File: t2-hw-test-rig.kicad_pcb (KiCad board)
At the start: 2 copper layers, 86.4 x 94 mm, 150 parts, among them J101 CONN_01X02, J102 BARREL_JACK, J103 CONN_01X02, J201 MICROUSB-TH, J202 CONN_01X02, J203 MICROUSB-TH, J204 USB_A_TH, J301 CONN_02x05, 0.05", Q101 pMOS, Q401 CJ2302, Q402 CJ2302, Q403 CJ2302, Q404 CJ2302, SW301 Switch_DPST, SW302 Switch_DPST, U101 MAX6102, U102 XC6206P332MR-G, U301 ATSAMD21J18A-MUT, U302 AAT4610, U303 AAT4610, U401 MAX9919FASA+, U402 MAX9919FASA+, U403 MAX9919FASA+, U404 MAX9919FASA+, U405 MAX9919FASA+, U501 TSV324IDT, U502 TSV324IDT, U503 TSV324IDT, X301 FC-135

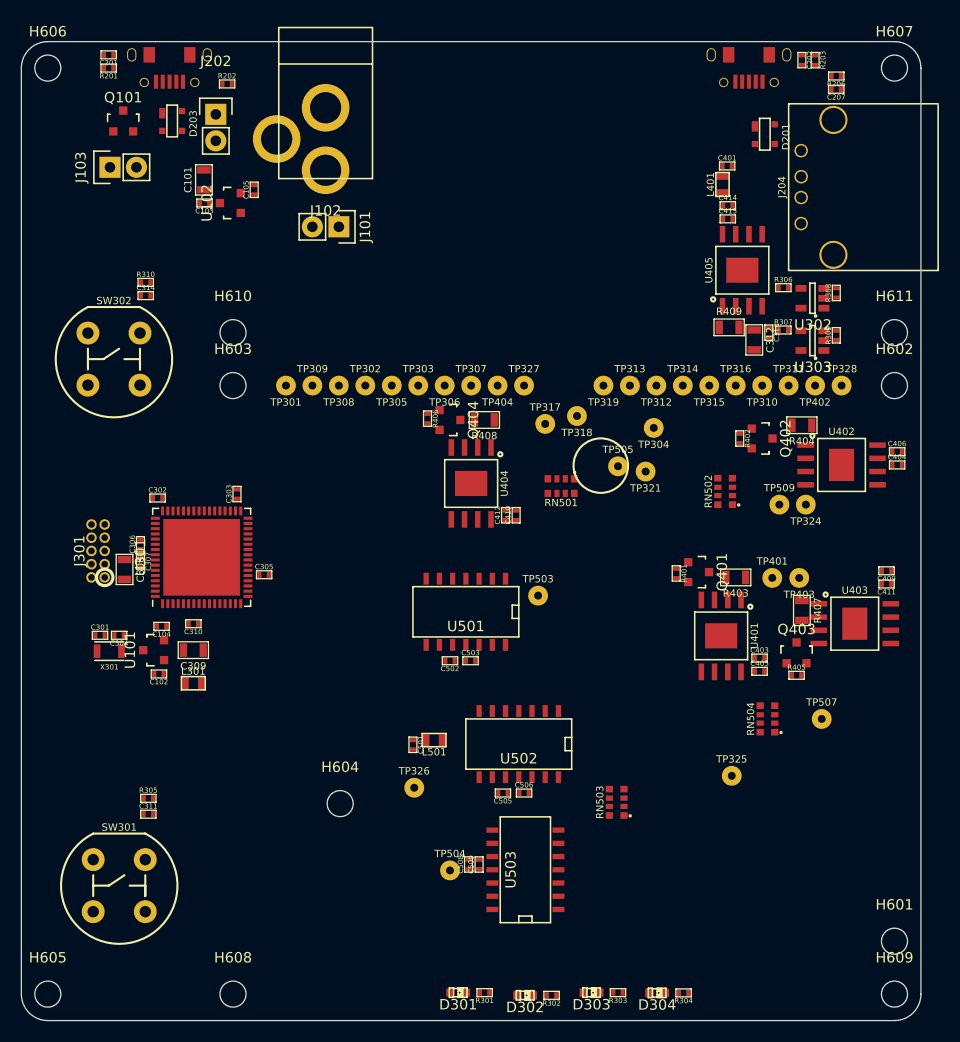
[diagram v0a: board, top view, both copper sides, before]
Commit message: mostly routed... time to go back and pin mux
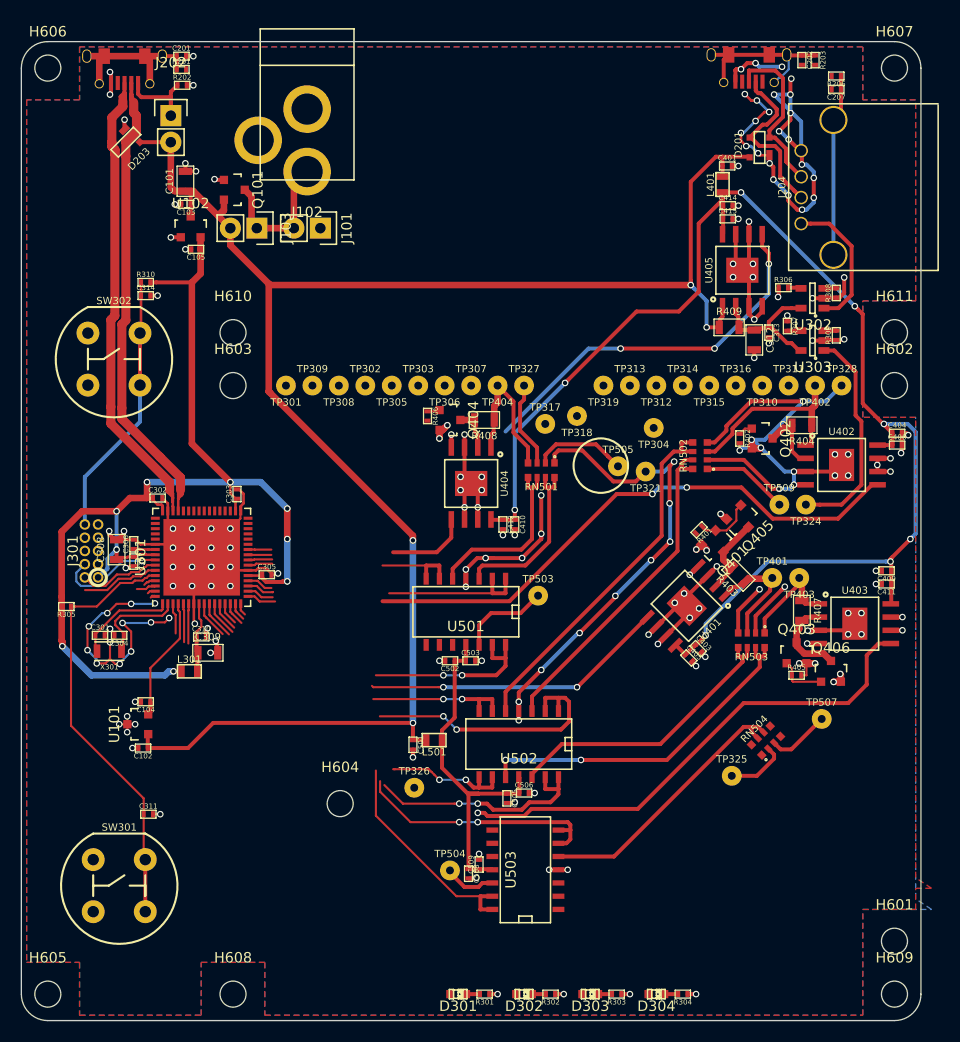
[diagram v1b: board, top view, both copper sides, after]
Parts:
- added Q405: CJ2302 DNP, Housings_SOT-23_SOT-143_TSOT-6:SOT-23, F.Cu at (119.9, 104.3)
- added Q406: CJ2302 DNP, Housings_SOT-23_SOT-143_TSOT-6:SOT-23, F.Cu at (128.5, 118.9)
- moved RN503 20.2 mm to (120.9, 115.9), turned to 180 degrees
- moved R305 20.0 mm to (55.1, 112.6), turned to 180 degrees
- moved J103 15.3 mm to (73.4, 76.3), turned to 270 degrees
- moved Q101 12.5 mm to (71.2, 72.6), turned to 270 degrees
- moved C105 7.99 mm to (67.6, 78.4), turned to 180 degrees
- moved C104 7.40 mm to (62.7, 121.8)
- moved U101 7.27 mm to (62.0, 124.0)
- moved C102 7.27 mm to (62.5, 126.2)
- moved C201 6.99 mm to (66.2, 59.8), turned to 0 degrees
- moved R201 6.99 mm to (66.2, 61.1), turned to 0 degrees
- moved C405 6.91 mm to (114.9, 117.6), turned to 315 degrees
- moved C403 5.96 mm to (115.8, 116.7), turned to 315 degrees
- moved D203 4.89 mm to (60.8, 68.1), turned to 225 degrees
- moved R401 4.73 mm to (115.9, 105.3), turned to 225 degrees
- moved U102 4.44 mm to (67.1, 76.2), turned to 0 degrees
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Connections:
- RN501 pad 1: UUT_33CP -> GND
- RN501 pad 2: GND -> UUT_33CP
- RN501 pad 3: UUT_33PB -> GND
- RN501 pad 4: GND -> UUT_33PB
- RN504 pad 2: UUT_33MT -> GND
- RN504 pad 3: GND -> UUT_33MT
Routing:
- net GND: track 0.00 -> 409.0 mm, vias 0 -> 181
- net +5V: track 0.00 -> 199.0 mm, vias 0 -> 4
- net /CURRENT/VCC_CSA: track 0.00 -> 129.6 mm, vias 0 -> 8
- net +3V3: track 0.00 -> 108.7 mm, vias 0 -> 9
- net I_PA33: track 0.00 -> 58.5 mm, vias 0 -> 2
- net SAM_USB_D+: track 0.00 -> 50.8 mm
- net I_USB1: track 0.00 -> 50.6 mm, vias 0 -> 1
- net SAM_USB_D-: track 0.00 -> 49.3 mm
- net /SAM/TEST_START_BUTTON: track 0.00 -> 41.6 mm
- net I_UUT: track 0.00 -> 40.5 mm, vias 0 -> 3
- net /OP AMPS/33PA_DIV: track 0.00 -> 35.4 mm
- net /OP AMPS/VDD_OPAMPS: track 0.00 -> 33.9 mm
- net /OP AMPS/5VUSB1_DIV: track 0.00 -> 33.4 mm, vias 0 -> 2
- net /OP AMPS/5V_DIV: track 0.00 -> 32.1 mm
- net I_USB0: track 0.00 -> 31.5 mm, vias 0 -> 2
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- added copper zone on B.Cu, net GND
- added copper zone on F.Cu, net GND
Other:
- net class Default: trace_width 0.254 -> 0.2032; via_drill 0.4572 -> 0.4064
- rule pad_to_mask_clearance: 0 -> 0.0762

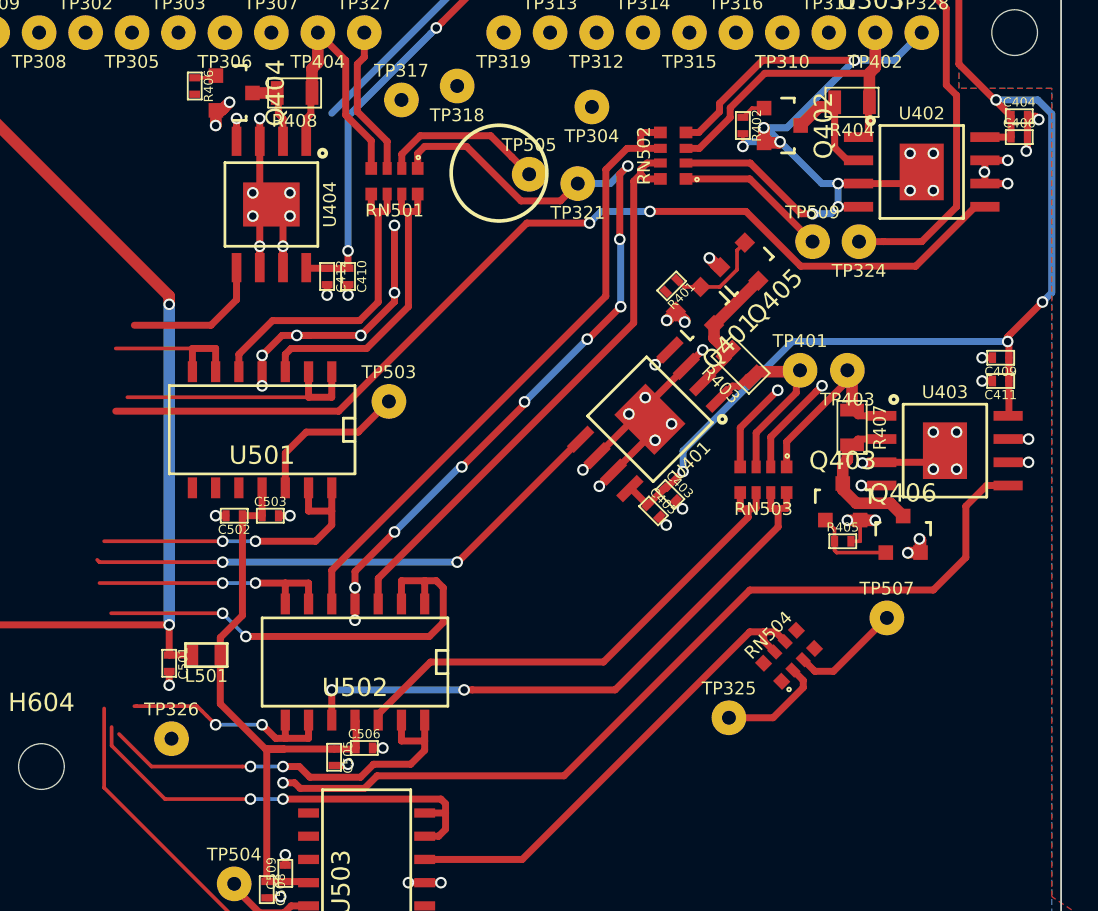
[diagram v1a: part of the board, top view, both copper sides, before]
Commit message: more analog pinswaps
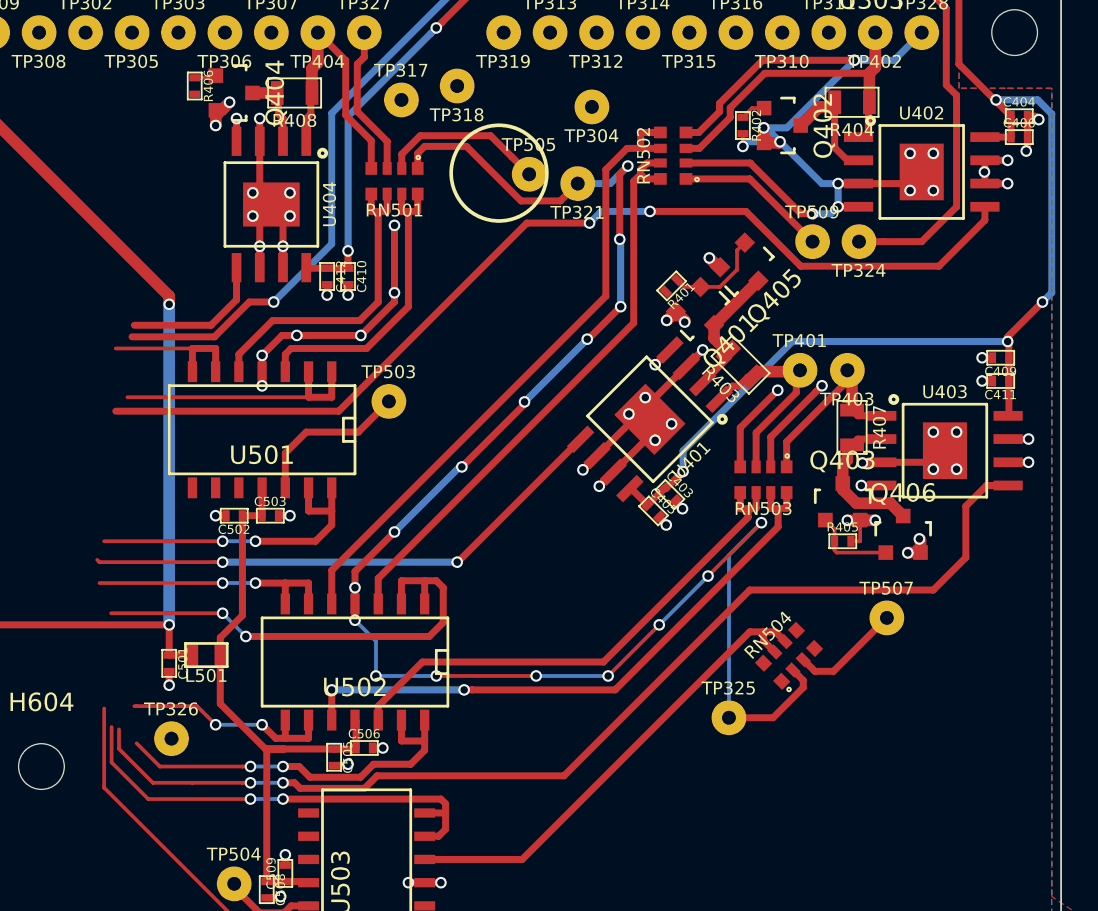
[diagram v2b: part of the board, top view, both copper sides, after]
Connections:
- U301 pad 10: 33PB_DIV_BUFF -> I_USB0
- U301 pad 12: 33CP_DIV_BUFF -> I_PA33
- U301 pad 13: I_USB0 -> 33CP_DIV_BUFF
- U301 pad 14: I_USB1 -> 33PB_DIV_BUFF
- U301 pad 15: 33PA_DIV_BUFF -> I_UUT
- U301 pad 16: 5V_DIV_BUFF -> I_PB33
- U301 pad 5: I_UUT -> 5VUSB1_DIV_BUFF
- U301 pad 6: I_PA33 -> 5V_DIV_BUFF
- U301 pad 61: 5VUSB0_DIV_BUFF -> 18_BUFF
- U301 pad 62: 5VUSB1_DIV_BUFF -> 33MT_DIV_BUFF
- U301 pad 63: 33MT_DIV_BUFF -> I_USB1
- U301 pad 64: 18_BUFF -> 5VUSB0_DIV_BUFF
- U301 pad 9: I_PB33 -> 33PA_DIV_BUFF
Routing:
- net GND: track 409.0 -> 448.4 mm, vias 181 -> 188
- net I_UUT: track 40.5 -> 58.7 mm, vias 3 -> 4
- net I_USB1: track 50.6 -> 59.9 mm, vias 1 -> 2
- net 5V_DIV_BUFF: track 27.1 -> 29.7 mm
- net I_PB33: track 11.6 -> 9.12 mm
- net 33PA_DIV_BUFF: track 15.5 -> 17.4 mm
- net 5VUSB0_DIV_BUFF: track 23.6 -> 21.7 mm
- net 5VUSB1_DIV_BUFF: track 14.1 -> 16.0 mm
- net 33MT_DIV_BUFF: track 25.2 -> 26.9 mm
- net I_USB0: track 31.5 -> 33.0 mm
- net 33PB_DIV_BUFF: track 11.7 -> 10.3 mm
- net 18_BUFF: track 21.6 -> 22.3 mm
- net 33CP_DIV_BUFF: track 16.8 -> 16.2 mm
- net I_PA33: track 58.5 -> 57.9 mm

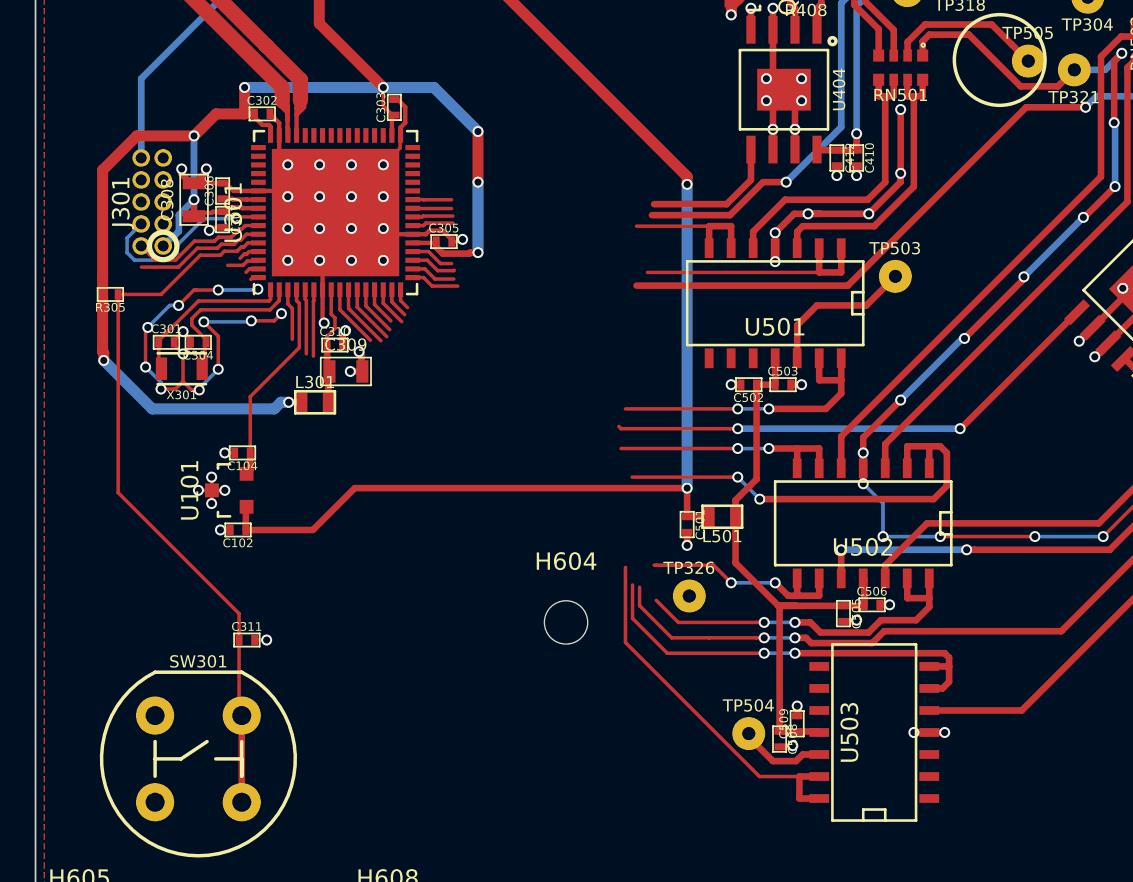
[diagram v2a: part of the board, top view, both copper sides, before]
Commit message: analog routed!
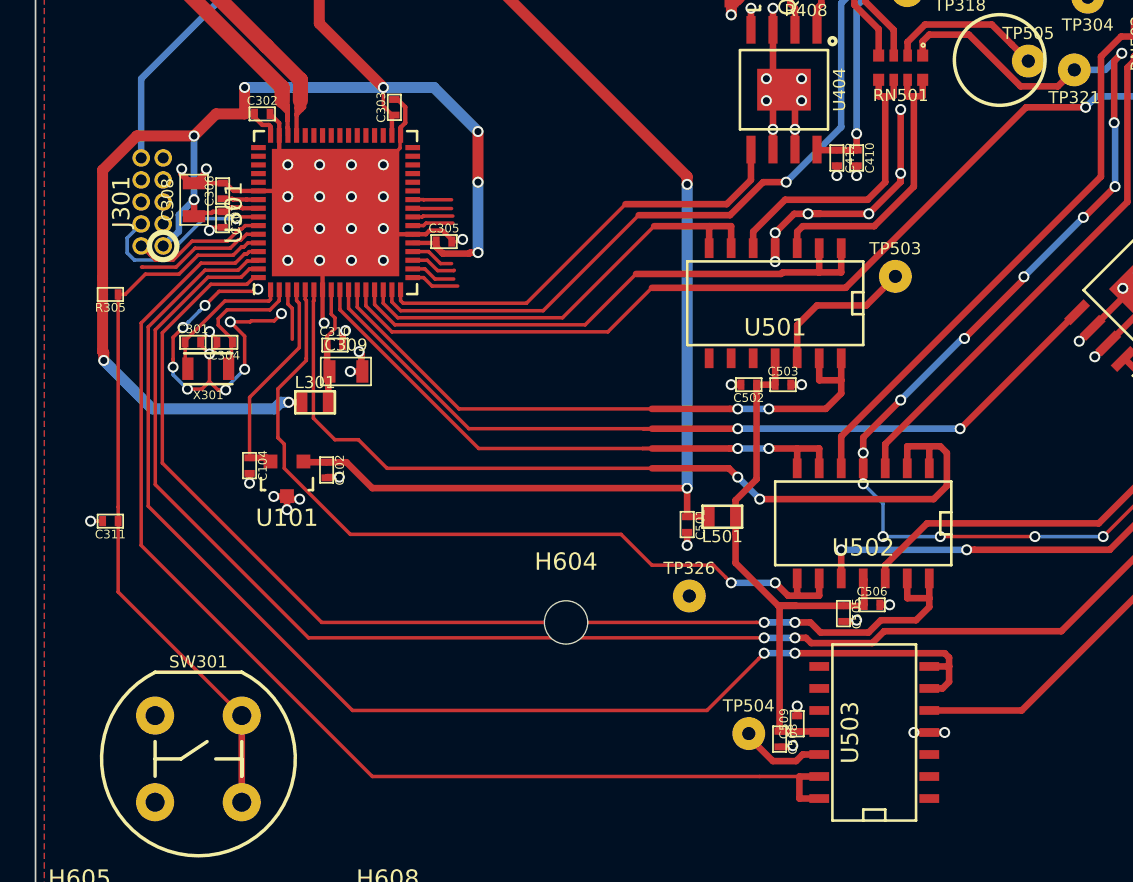
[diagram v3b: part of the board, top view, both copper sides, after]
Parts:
- moved C311 10.4 mm to (55.1, 125.7), turned to 180 degrees
- moved C102 6.17 mm to (67.6, 122.8), turned to 270 degrees
- moved U101 3.40 mm to (65.3, 123.3), turned to 180 degrees
- moved C301 1.52 mm to (59.9, 115.4)
- moved C304 1.52 mm to (61.7, 115.4)
- moved X301 1.52 mm to (60.8, 116.9)
- moved C104 0.84 mm to (63.1, 122.5), turned to 270 degrees
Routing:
- net 33MT_DIV_BUFF: track 26.9 -> 74.7 mm
- net 18_BUFF: track 22.3 -> 68.4 mm
- net 5VUSB0_DIV_BUFF: track 21.7 -> 67.7 mm
- net I_USB1: track 59.9 -> 105.2 mm
- net 5VUSB1_DIV_BUFF: track 16.0 -> 47.1 mm
- net 5V_DIV_BUFF: track 29.7 -> 53.1 mm
- net 33PA_DIV_BUFF: track 17.4 -> 34.8 mm
- net I_UUT: track 58.7 -> 75.2 mm
- net I_PB33: track 9.12 -> 25.6 mm
- net I_USB0: track 33.0 -> 49.2 mm
- net 33CP_DIV_BUFF: track 16.2 -> 32.3 mm
- net 33PB_DIV_BUFF: track 10.3 -> 25.9 mm
- net 12_BUFF: track 20.8 -> 36.3 mm
- net I_PA33: track 57.9 -> 73.3 mm
- net +5V: track 199.0 -> 193.9 mm
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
